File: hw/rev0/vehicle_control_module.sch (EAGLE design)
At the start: 190 parts, among them IC1 SJA1105TELY, IC10 TJA1100HNZ, IC11 KSZ8061MNXI-TR, IC12 TJA1100HNZ, IC2 ATSAMV71Q21B-AABT, IC3 TJA1100HNZ, IC4 FT2232HL, IC5 TRS3232EQPWRQ1, IC6 AT24MAC402-XHM-B, IC7 DS3231SN#, IC8 TLE9252VSKXUMA1, J1 2305018-2, J10 5-2337992-3, J12 1017505, J2 2305018-2, J3 1017505, J4 1017505, J5 1017505, J6 1017505, J7 1017505, J8 1017505, J9 1017505, U1 122-2920-GR, Y1 NX3225SA-25MHZ-EXS00A-CS11338, Y2 NX2016SA-25.000M-STD-CZS-1

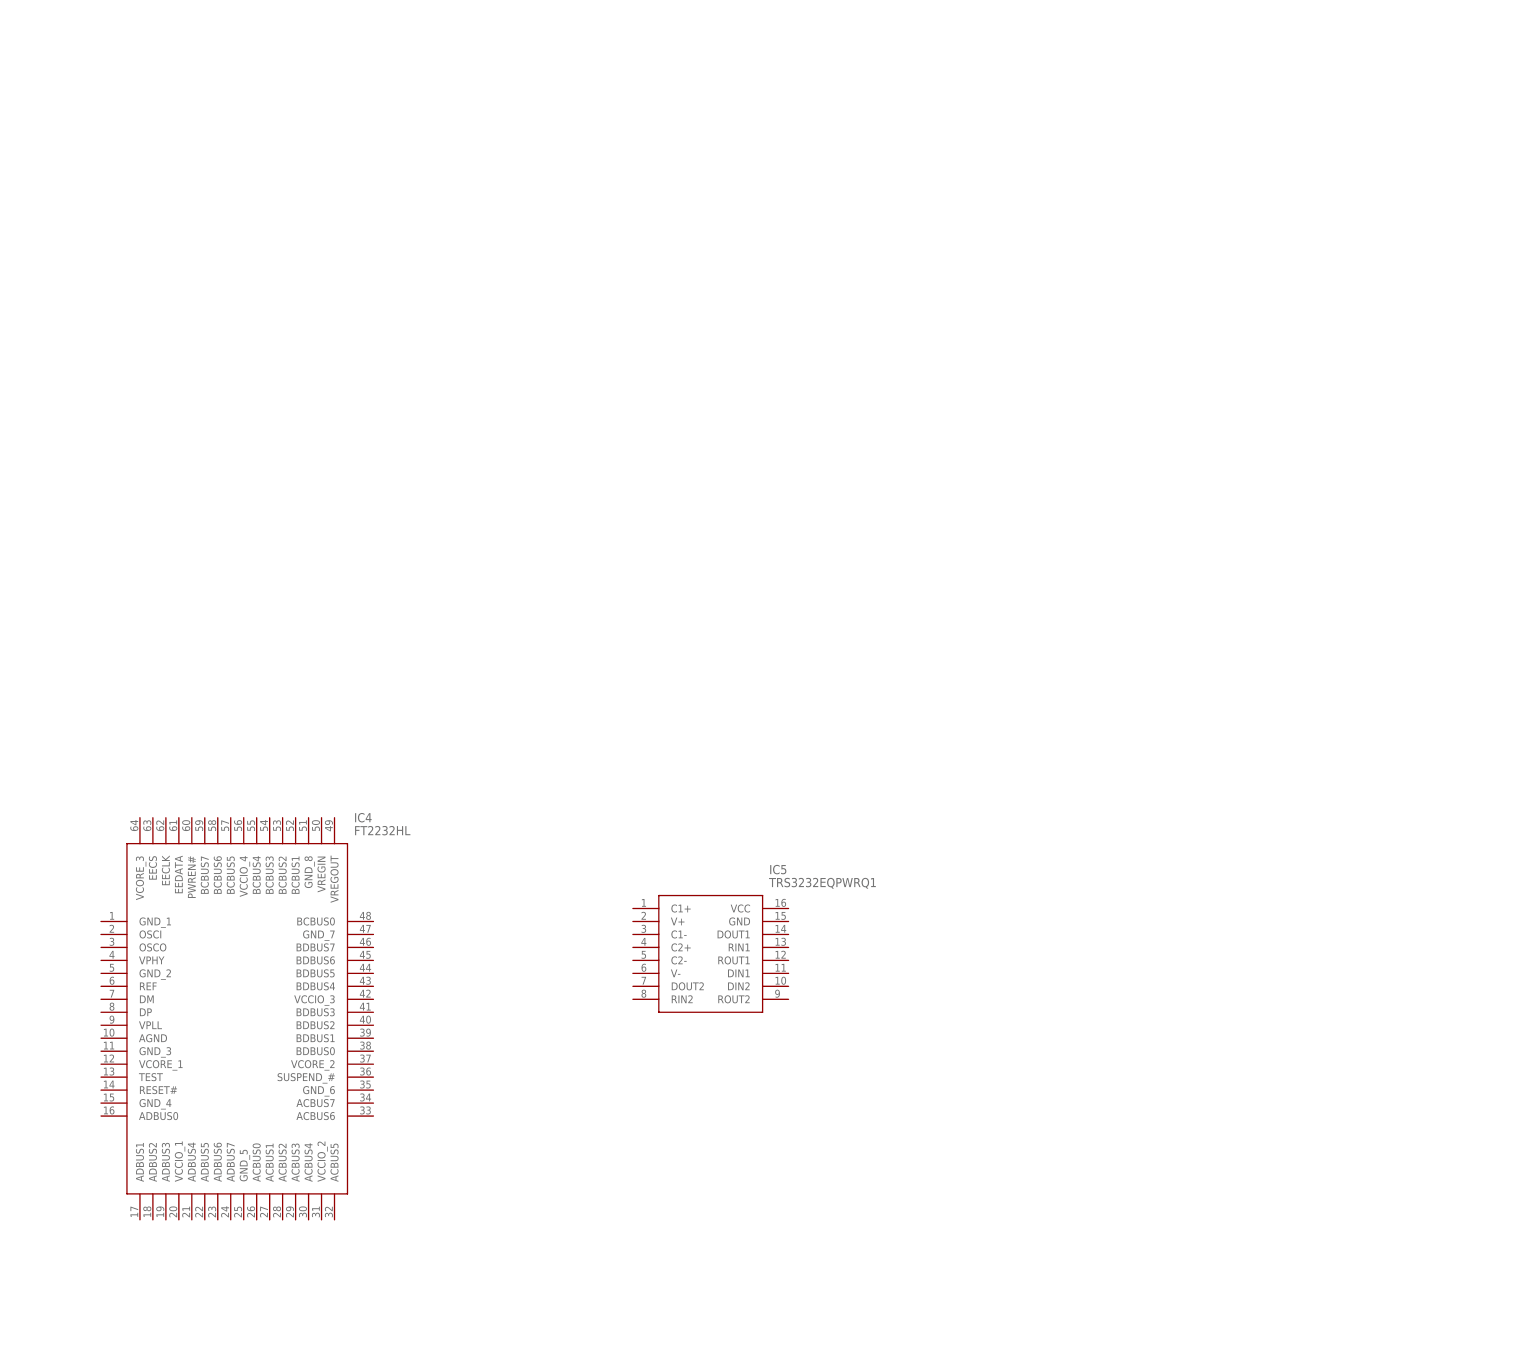
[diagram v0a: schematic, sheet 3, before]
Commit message: Swap EEPROM with QSPI Flash, still has 48-bit EUI
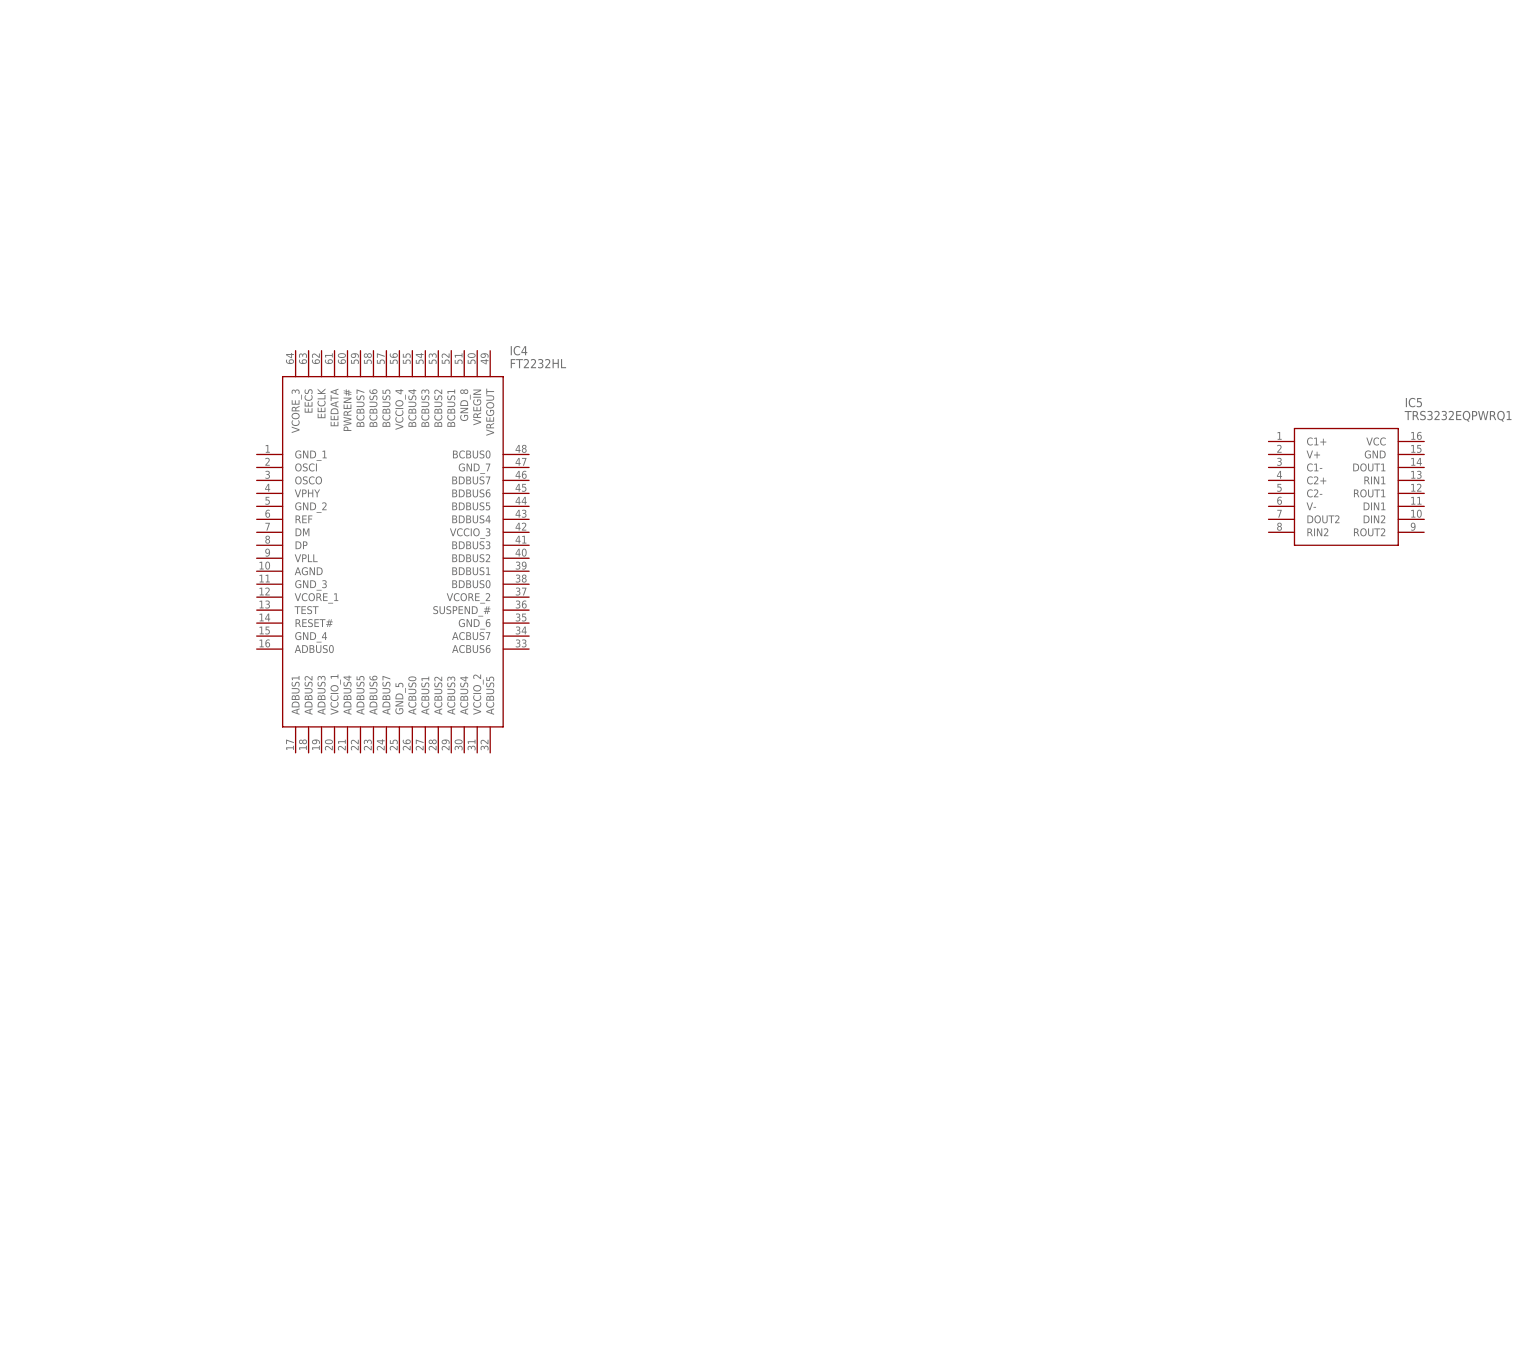
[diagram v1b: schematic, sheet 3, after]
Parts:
- added C64: 1uF, rcl:C-USC0603
- added R78: 0, rcl:R-US_R0603
- added R79, R80, R81: 4.7k, rcl:R-US_R0603
- IC6: value AT24MAC402-XHM-B -> SST26VF032BT-104I_SM; device samacsys:AT24MAC402-XHM-B -> samacsys:SST26VF032BT-104I_SM
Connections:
- new net EXTINT_RTC: IC2.PA0, IC7.!INT!/SQW, R81.1
- new net FLASH_WP: IC2.PC4, IC6.WP#/SIO2, R78.1
- new net QSPI_QCS: IC2.PA11, IC6.CE#
- new net QSPI_QIO0: IC2.PA13, IC6.SI/SIO0
- new net QSPI_QIO1: IC2.PA12, IC6.SO/SIO1
- new net QSPI_QSCK: IC2.PA14, IC6.SCK
- net +3V3: now also C64.1, IC6.HOLD/SIO3, IC6.VDD, IC7.VCC, R78.2, R79.2, R80.2, R81.2
- net GND: now also C64.2, IC6.VSS, IC7.GND, IC7.NC_1, IC7.NC_2, IC7.NC_3, IC7.NC_4, IC7.NC_5, IC7.NC_6, IC7.NC_7, IC7.NC_8, U1.3
- net I2C0_TWCK: now also IC7.SCL, R79.1
- net I2C0_TWD: now also IC7.SDA, R80.1
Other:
- moved on the sheet: IC4, IC5, IC6, IC7, U1
